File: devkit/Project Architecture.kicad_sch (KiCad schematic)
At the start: 0 parts

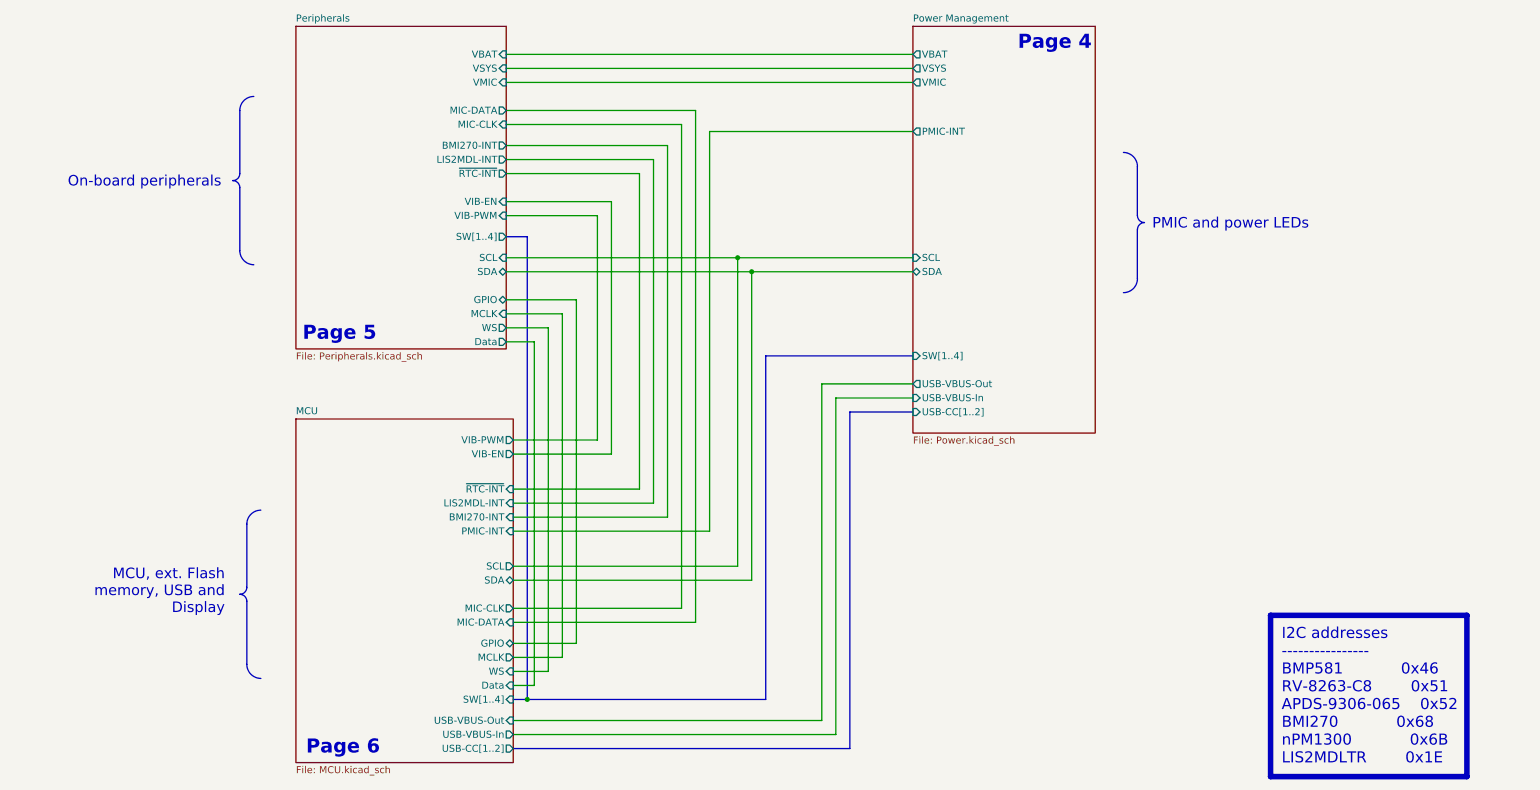
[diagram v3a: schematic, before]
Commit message: Revert "Fix wrong page numbers in Project Architecture schematic"
This reverts commit 85922ebd93d309191d5d3522e6a6ede7ddadbc08.
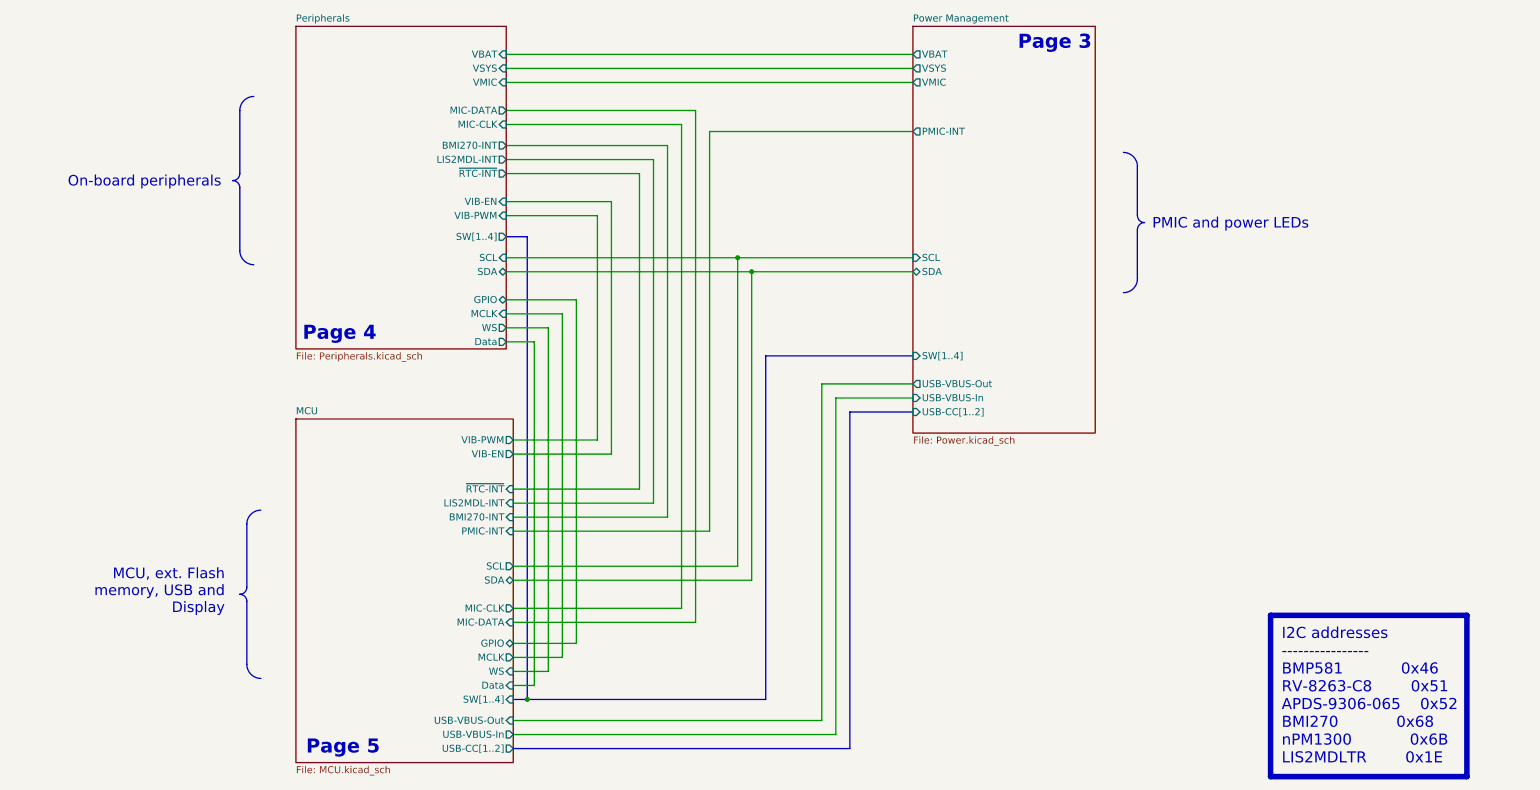
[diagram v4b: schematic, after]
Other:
- note added: "Page 3"
- note removed: "Page 6"
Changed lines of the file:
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@@
 		)
 	)
-	(text "Page 6"
+	(text "Page 5"
 		(exclude_from_sim no)
 		(at 86.36 151.13 0)
@@
 			)
 			(justify right bottom)
-			(href "#6")
+			(href "#5")
+		)
+	)
+	(text "Page 3"
+		(exclude_from_sim no)
+		(at 215.265 23.495 0)
+		(effects
+			(font
+				(size 2.54 2.54)
+				(bold yes)
+				(color 20 60 40 1)
+			)
+			(justify right bottom)
+			(href "#3")
 		)
 	)
 	(text "Page 4"
 		(exclude_from_sim no)
-		(at 215.265 23.495 0)
+		(at 85.725 76.2 0)
 		(effects
 			(font
@@
 		)
 	)
-	(text "Page 5"
-		(exclude_from_sim no)
-		(at 85.725 76.2 0)
-		(effects
-			(font
-				(size 2.54 2.54)
-				(bold yes)
-				(color 20 60 40 1)
-			)
-			(justify right bottom)
-			(href "#5")
-		)
-	)
